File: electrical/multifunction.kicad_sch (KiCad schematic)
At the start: 8 parts

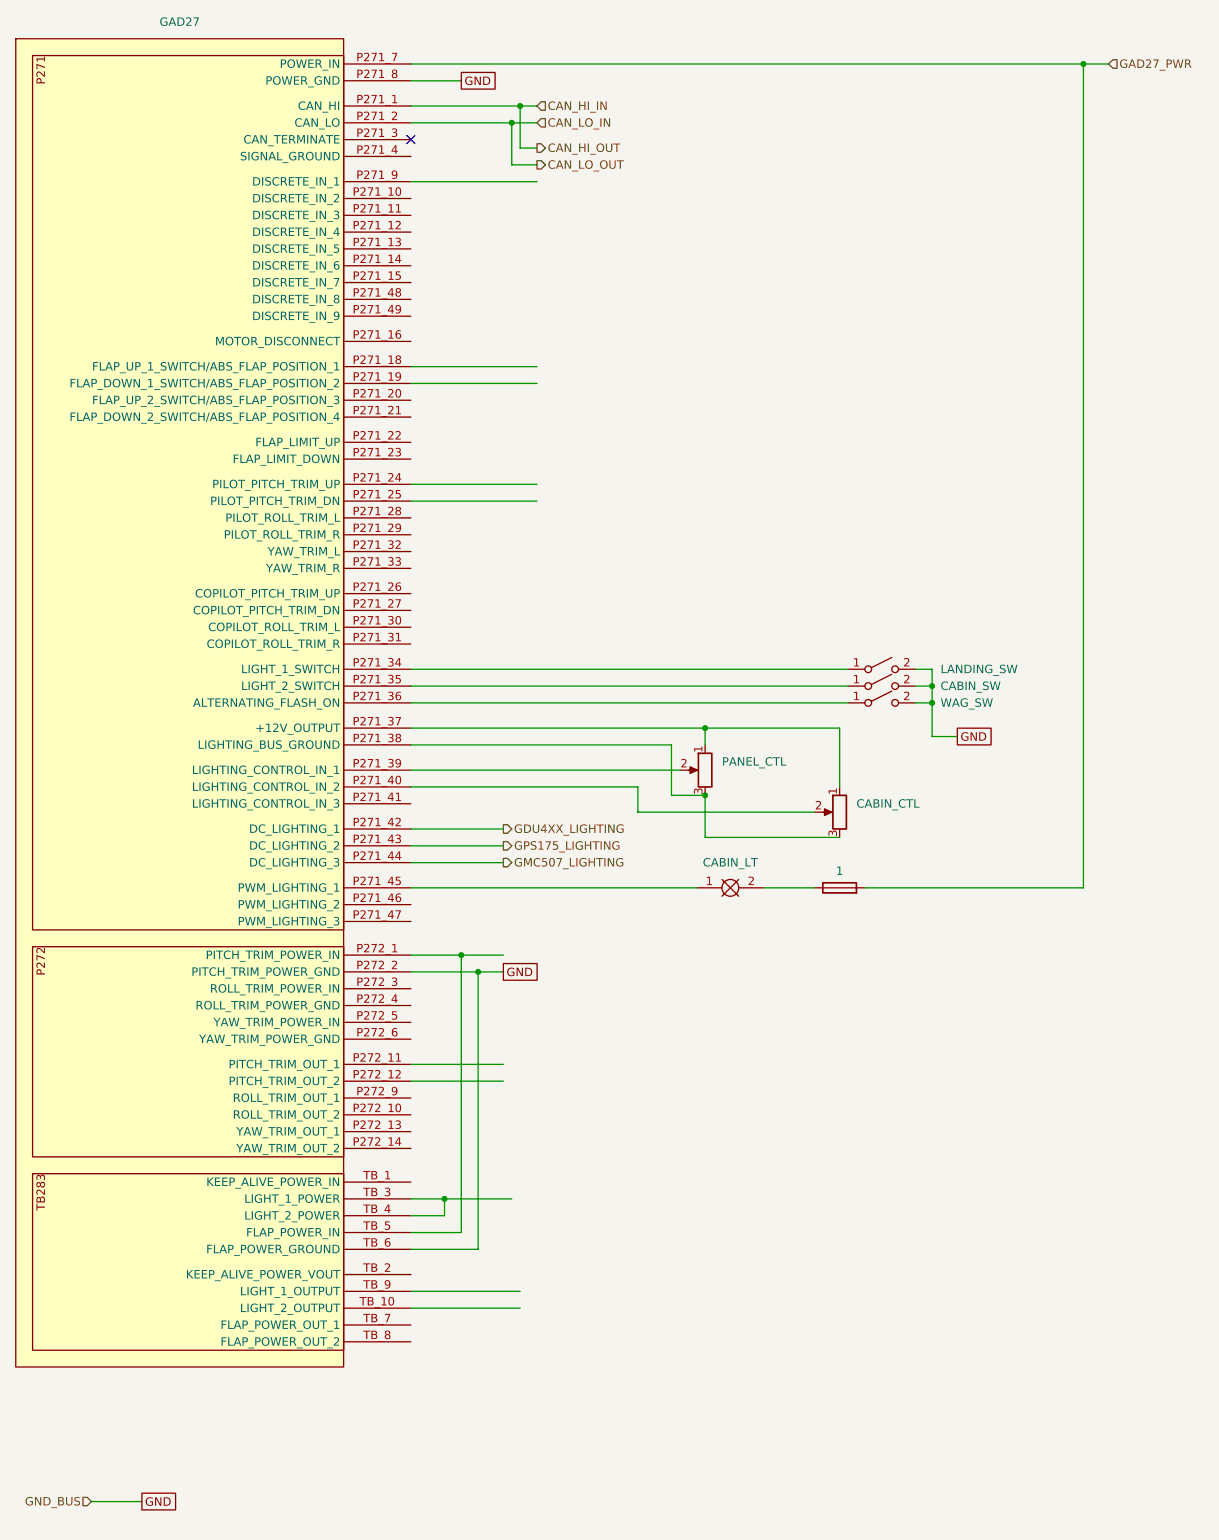
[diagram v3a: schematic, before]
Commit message: Converted to breakers w/GAD 27 instead of VP-X.
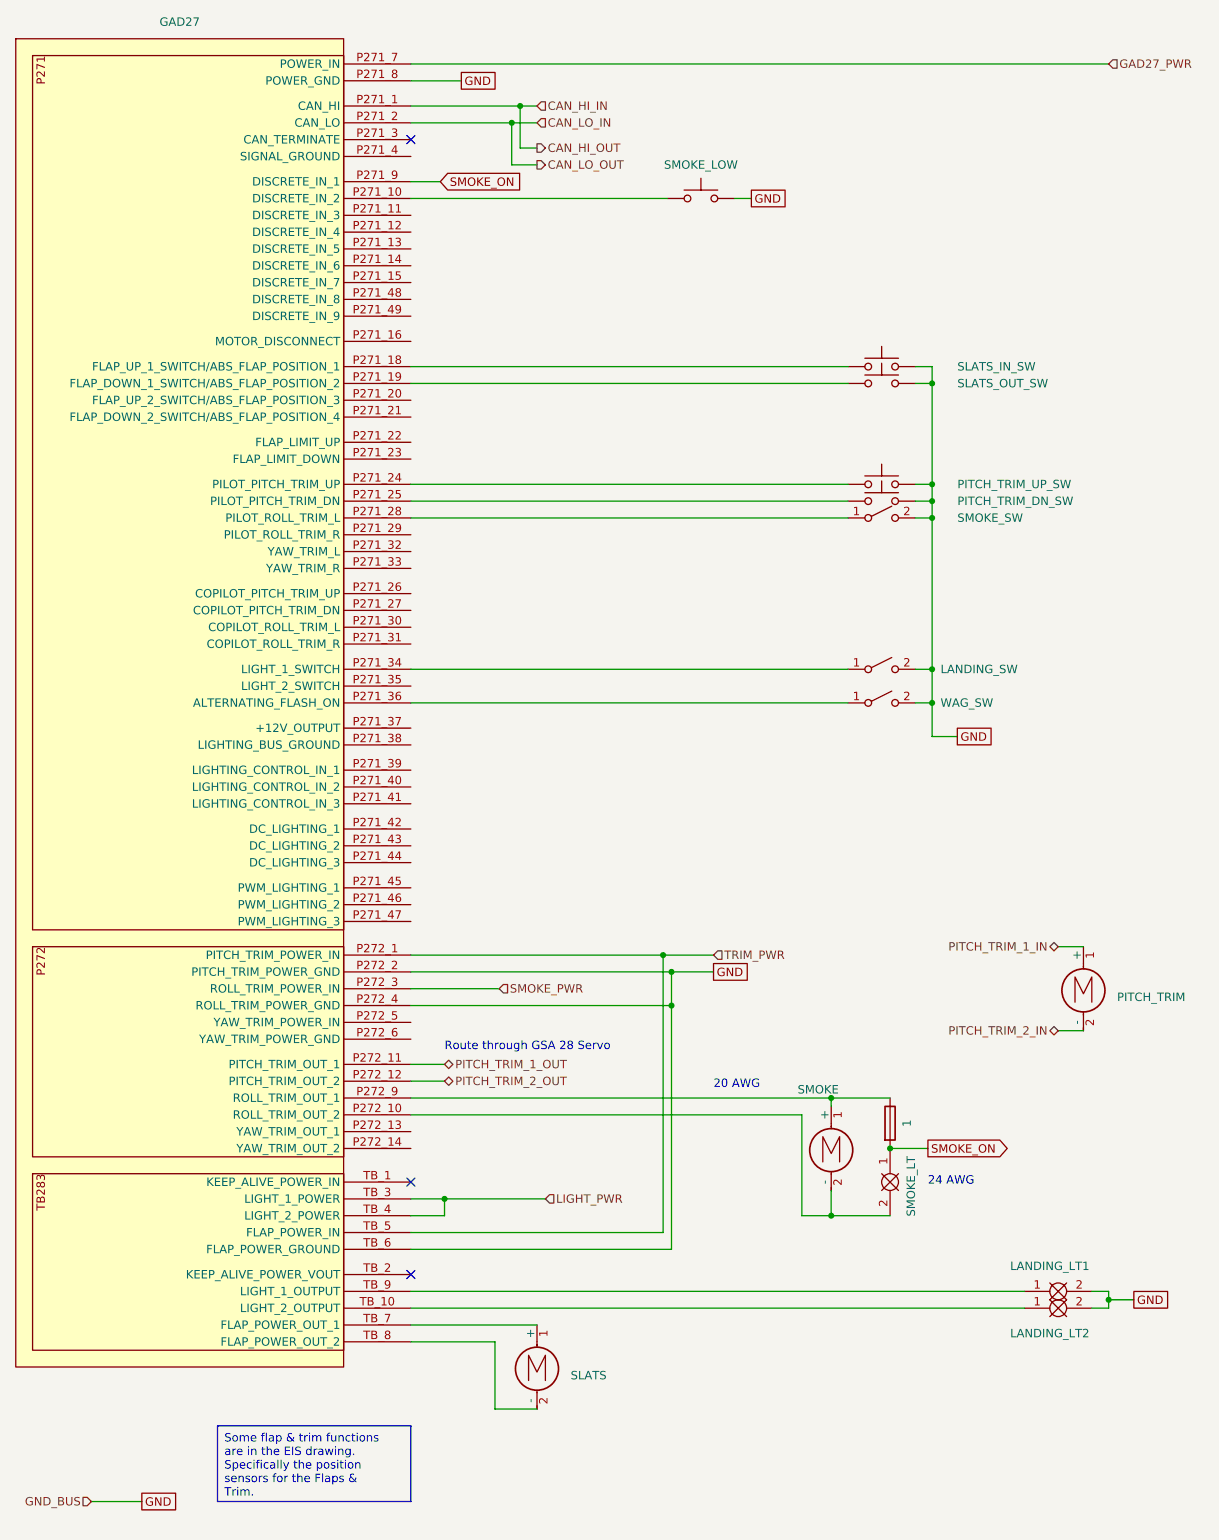
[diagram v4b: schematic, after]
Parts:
- removed CABIN_CTL, PANEL_CTL: LIGHTS_REOSTAT, symbol Device:R_Potentiometer
- removed CABIN_LT: ~, symbol flyerx:Bulb
- removed CABIN_LT_FS: 1, symbol Device:Fuse
- removed CABIN_SW: ~, symbol Switch:SW_SPST
- added LANDING_LT1, LANDING_LT2, SMOKE_LT: ~, symbol flyerx:Bulb
- added PITCH_TRIM, SLATS, SMOKE: Motor_DC, symbol Motor:Motor_DC
- added PITCH_TRIM_DN_SW, PITCH_TRIM_UP_SW, SLATS_IN_SW, SLATS_OUT_SW: SW_Push, symbol Switch:SW_Push
- added SMOKE_LOW: FLOAT_SENSOR, symbol Switch:SW_Push
- added SMOKE_LT_FS: 1, symbol Device:Fuse
- added SMOKE_SW: ~, symbol Switch:SW_SPST
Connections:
- net GND: now also GAD27.P272_4 (ROLL_TRIM_POWER_GND), LANDING_LT1.2, LANDING_LT2.2, PITCH_TRIM_DN_SW.2, PITCH_TRIM_UP_SW.2, SLATS_IN_SW.2, SLATS_OUT_SW.2, SMOKE_LOW.2, SMOKE_SW.2 (B)
- net at GAD27.P271_10 (DISCRETE_IN_2): now also SMOKE_LOW.1
- net at GAD27.P271_18 (FLAP_UP_1_SWITCH/ABS_FLAP_POSITION_1): now also SLATS_IN_SW.1
- net at GAD27.P271_19 (FLAP_DOWN_1_SWITCH/ABS_FLAP_POSITION_2): now also SLATS_OUT_SW.1
- net at GAD27.P271_24 (PILOT_PITCH_TRIM_UP): now also PITCH_TRIM_UP_SW.1
- net at GAD27.P271_25 (PILOT_PITCH_TRIM_DN): now also PITCH_TRIM_DN_SW.1
- net at GAD27.P271_28 (PILOT_ROLL_TRIM_L): now also SMOKE_SW.1 (A)
- net SMOKE_ON: now reaches GAD27.P271_9 (DISCRETE_IN_1)
- net SMOKE_ON: now also SMOKE_LT.1, SMOKE_LT_FS.2
- net TRIM_PWR: now reaches GAD27.P272_1 (PITCH_TRIM_POWER_IN), GAD27.TB_5 (FLAP_POWER_IN)
- net at GAD27.P272_10 (ROLL_TRIM_OUT_2): now also SMOKE.2 (-), SMOKE_LT.2
- net PITCH_TRIM_1_OUT: now reaches GAD27.P272_11 (PITCH_TRIM_OUT_1)
- net PITCH_TRIM_2_OUT: now reaches GAD27.P272_12 (PITCH_TRIM_OUT_2)
- net SMOKE_PWR: now reaches GAD27.P272_3 (ROLL_TRIM_POWER_IN)
- net at GAD27.P272_9 (ROLL_TRIM_OUT_1): now also SMOKE.1 (+), SMOKE_LT_FS.1
- net at GAD27.TB_10 (LIGHT_2_OUTPUT): now also LANDING_LT2.1
- net LIGHT_PWR: now reaches GAD27.TB_3 (LIGHT_1_POWER), GAD27.TB_4 (LIGHT_2_POWER)
- net at GAD27.TB_7 (FLAP_POWER_OUT_1): now also SLATS.1 (+)
- net at GAD27.TB_8 (FLAP_POWER_OUT_2): now also SLATS.2 (-)
- net at GAD27.TB_9 (LIGHT_1_OUTPUT): now also LANDING_LT1.1
- net GDU4XX_LIGHTING: no longer names the net of GAD27.P271_42 (DC_LIGHTING_1)
- net GMC507_LIGHTING: no longer names the net of GAD27.P271_44 (DC_LIGHTING_3)
- net GPS175_LIGHTING: no longer names the net of GAD27.P271_43 (DC_LIGHTING_2)
- new net PITCH_TRIM_1_IN: PITCH_TRIM.1 (+)
- new net PITCH_TRIM_2_IN: PITCH_TRIM.2 (-)
- no-connect marks 1 -> 3
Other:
- note added: "20 AWG"
- note added: "24 AWG"
- note added: "Route through GSA 28 Servo"

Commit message: Unknown set of changes. Didn't spent time to look
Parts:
- added GHA15_DISABLE_SW: ~, symbol Switch:SW_SPST
- renumbered SMOKE_LOW to SMOKE_LOW_SW
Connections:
- net PITCH_TRIM_1_OUT is gone; now on an unnamed net: GAD27.P272_11 (PITCH_TRIM_OUT_1)
- net PITCH_TRIM_2_OUT is gone; now on an unnamed net: GAD27.P272_12 (PITCH_TRIM_OUT_2)
- net GND: now also GHA15_DISABLE_SW.2 (B)
- net at GAD27.P271_11 (DISCRETE_IN_3): now also GHA15_DISABLE_SW.1 (A)
- net PITCH_TRIM_1_IN: no longer names the net of PITCH_TRIM.1 (+)
- net PITCH_TRIM_2_IN: no longer names the net of PITCH_TRIM.2 (-)
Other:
- note added: "Too much power to route through servo."
- note removed: "Route through GSA 28 Servo"
- moved on the sheet: PITCH_TRIM
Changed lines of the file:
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@@
     (title "Flaps, Lights & Trim")
     (date "2024-02-08")
-    (rev "1.0")
+    (rev "1.0.1")
     (company "N915SN Angry Bird")
     (comment 1 "w/Breakers")
@@
   )
   (junction (at 97.79 33.02) (diameter 0) (color 0 0 0 0)
+  )
+  (junction (at 133.35 49.53) (diameter 0) (color 0 0 0 0)
   )
   (junction (at 160.02 74.93) (diameter 0) (color 0 0 0 0)
@@
     (stroke (width 0) (type default))
   )
+  (wire (pts (xy 177.165 180.34) (xy 177.165 190.5))
+    (stroke (width 0) (type default))
+  )
   (wire (pts (xy 86.36 200.66) (xy 86.36 198.12))
     (stroke (width 0) (type default))
@@
     (stroke (width 0) (type default))
   )
-  (wire (pts (xy 81.28 180.34) (xy 86.36 180.34))
-    (stroke (width 0) (type default))
-  )
   (wire (pts (xy 81.28 212.09) (xy 173.99 212.09))
     (stroke (width 0) (type default))
@@
     (stroke (width 0) (type default))
   )
+  (wire (pts (xy 133.35 49.53) (xy 133.35 46.99))
+    (stroke (width 0) (type default))
+  )
   (wire (pts (xy 144.78 182.88) (xy 153.67 182.88))
     (stroke (width 0) (type default))
@@
     (stroke (width 0) (type default))
   )
+  (wire (pts (xy 81.28 180.34) (xy 177.165 180.34))
+    (stroke (width 0) (type default))
+  )
   (wire (pts (xy 160.02 90.17) (xy 160.02 92.71))
     (stroke (width 0) (type default))
@@
     (stroke (width 0) (type default))
   )
+  (wire (pts (xy 81.28 49.53) (xy 120.015 49.53))
+    (stroke (width 0) (type default))
+  )
   (wire (pts (xy 186.69 213.36) (xy 190.5 213.36))
     (stroke (width 0) (type default))
@@
     (stroke (width 0) (type default))
   )
-  (wire (pts (xy 81.28 177.8) (xy 86.36 177.8))
+  (wire (pts (xy 81.28 177.8) (xy 182.88 177.8))
     (stroke (width 0) (type default))
   )
@@
     (stroke (width 0) (type default))
   )
-  (wire (pts (xy 179.07 172.72) (xy 182.88 172.72))
-    (stroke (width 0) (type default))
-  )
   (wire (pts (xy 81.28 161.29) (xy 119.38 161.29))
     (stroke (width 0) (type default))
@@
     (stroke (width 0) (type default))
   )
-  (wire (pts (xy 130.175 46.99) (xy 132.715 46.99))
+  (wire (pts (xy 133.35 54.61) (xy 137.795 54.61))
     (stroke (width 0) (type default))
   )
@@
     (stroke (width 0) (type default))
   )
-  (wire (pts (xy 179.07 160.02) (xy 182.88 160.02))
-    (stroke (width 0) (type default))
-  )
   (wire (pts (xy 140.335 185.42) (xy 140.335 200.66))
     (stroke (width 0) (type default))
@@
     (stroke (width 0) (type default))
   )
+  (wire (pts (xy 133.35 54.61) (xy 133.35 49.53))
+    (stroke (width 0) (type default))
+  )
   (wire (pts (xy 119.38 161.29) (xy 127 161.29))
     (stroke (width 0) (type default))
   )
+  (wire (pts (xy 177.165 190.5) (xy 182.88 190.5))
+    (stroke (width 0) (type default))
+  )
   (wire (pts (xy 160.02 128.27) (xy 160.02 123.19))
     (stroke (width 0) (type default))
   )
+  (wire (pts (xy 133.35 46.99) (xy 130.175 46.99))
+    (stroke (width 0) (type default))
+  )
   (wire (pts (xy 157.48 92.71) (xy 160.02 92.71))
     (stroke (width 0) (type default))
@@
   )
   (wire (pts (xy 160.02 128.27) (xy 163.83 128.27))
+    (stroke (width 0) (type default))
+  )
+  (wire (pts (xy 130.175 49.53) (xy 133.35 49.53))
     (stroke (width 0) (type default))
   )
@@
     (effects (font (size 1.27 1.27)) (justify left top))
   )
-  (text "20 AWG" (at 127 181.61 0)
+  (text "20 AWG" (at 130.175 177.165 0)
     (effects (font (size 1.27 1.27)) (justify left bottom))
   )
@@
     (effects (font (size 1.27 1.27)) (justify left bottom))
   )
-  (text "Route through GSA 28 Servo" (at 86.36 175.895 0)
+  (text "Too much power to route through servo." (at 146.685 175.895 0)
     (effects (font (size 1.27 1.27)) (justify left bottom))
   )
@@
     )
   )
-  (global_label "GND" (shape passive) (at 132.715 46.99 0) (fields_autoplaced)
-    (effects (font (size 1.27 1.27)) (justify left))
-    (property "Intersheetrefs" "${INTERSHEET_REFS}" (at 138.4594 46.99 0)
+  (global_label "GND" (shape passive) (at 137.795 54.61 0) (fields_autoplaced)
+    (effects (font (size 1.27 1.27)) (justify left))
+    (property "Intersheetrefs" "${INTERSHEET_REFS}" (at 143.5394 54.61 0)
       (effects (font (size 1.27 1.27)) (justify left) hide)
     )
@@
     (effects (font (size 1.27 1.27)) (justify left))
   )
-  (hierarchical_label "PITCH_TRIM_1_OUT" (shape bidirectional) (at 86.36 177.8 0) (fields_autoplaced)
-    (effects (font (size 1.27 1.27)) (justify left))
-  )
   (hierarchical_label "SMOKE_PWR" (shape input) (at 94.615 166.37 0) (fields_autoplaced)
     (effects (font (size 1.27 1.27)) (justify left))
   )
-  (hierarchical_label "PITCH_TRIM_1_IN" (shape bidirectional) (at 179.07 160.02 180) (fields_autoplaced)
-    (effects (font (size 1.27 1.27)) (justify right))
-  )
   (hierarchical_label "GAD27_PWR" (shape input) (at 186.69 26.67 0) (fields_autoplaced)
     (effects (font (size 1.27 1.27)) (justify left))
   )
   (hierarchical_label "CAN_HI_OUT" (shape output) (at 100.33 39.37 0) (fields_autoplaced)
-    (effects (font (size 1.27 1.27)) (justify left))
-  )
-  (hierarchical_label "PITCH_TRIM_2_OUT" (shape bidirectional) (at 86.36 180.34 0) (fields_autoplaced)
     (effects (font (size 1.27 1.27)) (justify left))
   )
@@
   (hierarchical_label "TRIM_PWR" (shape input) (at 127 161.29 0) (fields_autoplaced)
     (effects (font (size 1.27 1.27)) (justify left))
-  )
-  (hierarchical_label "PITCH_TRIM_2_IN" (shape bidirectional) (at 179.07 172.72 180) (fields_autoplaced)
-    (effects (font (size 1.27 1.27)) (justify right))
   )
   (symbol (lib_id "flyerx:Garmin_GAD27") (at 21.59 22.86 0) (unit 1)
@@
   (symbol (lib_id "Switch:SW_Push") (at 125.095 46.99 0) (unit 1)
     (in_bom yes) (on_board yes) (dnp no)
-    (property "Reference" "SMOKE_LOW" (at 125.095 41.91 0)
+    (property "Reference" "SMOKE_LOW_SW" (at 144.145 45.085 0)
       (effects (font (size 1.27 1.27)))
     )
@@
       (project "electrical"
         (path "/e8ec215a-dbe2-4eba-a577-e50a0a128049/1b135381-3ea1-4e14-ae97-d4f35cdfb602"
-          (reference "SMOKE_LOW") (unit 1)
+          (reference "SMOKE_LOW_SW") (unit 1)
         )
       )
@@
     )
   )
-  (symbol (lib_id "Motor:Motor_DC") (at 182.88 165.1 0) (unit 1)
+  (symbol (lib_id "Motor:Motor_DC") (at 182.88 182.88 0) (unit 1)
     (in_bom yes) (on_board yes) (dnp no) (fields_autoplaced)
-    (property "Reference" "PITCH_TRIM" (at 187.96 167.64 0)
-      (effects (font (size 1.27 1.27)) (justify left))
-    )
-    (property "Value" "Motor_DC" (at 187.96 168.91 0)
-      (effects (font (size 1.27 1.27)) (justify left) hide)
-    )
-    (property "Footprint" "" (at 182.88 167.386 0)
-      (effects (font (size 1.27 1.27)) hide)
-    )
-    (property "Datasheet" "~" (at 182.88 167.386 0)
+    (property "Reference" "PITCH_TRIM" (at 187.96 185.42 0)
+      (effects (font (size 1.27 1.27)) (justify left))
+    )
+    (property "Value" "Motor_DC" (at 187.96 186.69 0)
+      (effects (font (size 1.27 1.27)) (justify left) hide)
+    )
+    (property "Footprint" "" (at 182.88 185.166 0)
+      (effects (font (size 1.27 1.27)) hide)
+    )
+    (property "Datasheet" "~" (at 182.88 185.166 0)
       (effects (font (size 1.27 1.27)) hide)
     )
@@
         )
       )
+    )
+  )
+  (symbol (lib_id "Switch:SW_SPST") (at 125.095 49.53 0) (unit 1)
+    (in_bom yes) (on_board yes) (dnp no)
+    (property "Reference" "GHA15_DISABLE_SW" (at 136.525 49.53 0)
+      (effects (font (size 1.27 1.27)) (justify left))
+    )
+    (property "Value" "~" (at 125.095 45.72 0)
+      (effects (font (size 1.27 1.27)))
+    )
+    (property "Footprint" "" (at 125.095 49.53 0)
+      (effects (font (size 1.27 1.27)) hide)
+    )
+    (property "Datasheet" "~" (at 125.095 49.53 0)
+      (effects (font (size 1.27 1.27)) hide)
+    )
+    (pin "2")
+    (pin "1")
+    (instances
+      (project "electrical"
+        (path "/e8ec215a-dbe2-4eba-a577-e50a0a128049/1b135381-3ea1-4e14-ae97-d4f35cdfb602"
+          (reference "GHA15_DISABLE_SW") (unit 1)
+        )
+      )
